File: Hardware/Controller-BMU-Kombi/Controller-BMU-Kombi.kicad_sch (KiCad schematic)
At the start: 45 parts, among them J1 Conn_01x05_Socket, J10 Conn_01x03_Pin, J11 Conn_01x03_Pin, J12 Conn_01x03_Pin, J13 Conn_01x03_Pin, J14 Conn_01x03_Pin, J15 Conn_01x03_Pin, J16 Conn_01x03_Pin, J17 Conn_01x03_Pin, J18 Conn_01x03_Pin, J19 Conn_01x03_Pin, J2 Conn_01x05_Socket, J20 Conn_01x03_Pin, J21 Conn_01x03_Pin, J22 Conn_01x03_Pin, J23 Conn_01x03_Pin, J24 Conn_01x03_Pin, J25 Conn_01x03_Socket, J26 Conn_01x04_Socket, J3 Conn_01x05_Socket, J4 Conn_01x05_Socket, J5 Conn_01x05_Socket, J6 Conn_01x05_Socket, J7 Conn_01x03_Pin, J8 Conn_01x03_Pin, J9 Conn_01x03_Pin, U2 ESP32_NODEMCU, U9 PCA9555PW

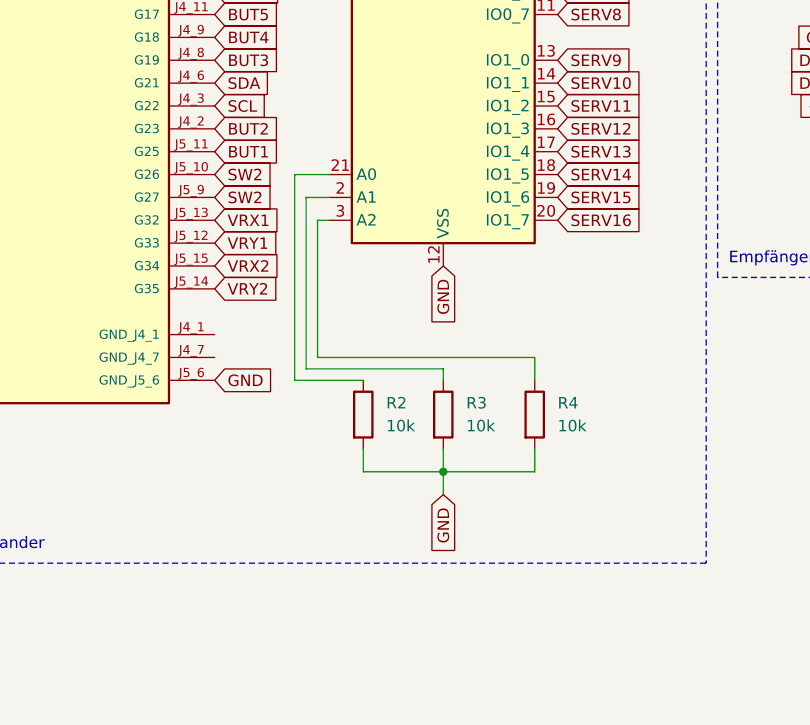
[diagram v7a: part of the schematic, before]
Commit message: Finished Controller-BMU-Kombi PCB
routing finished + finishing touches applied
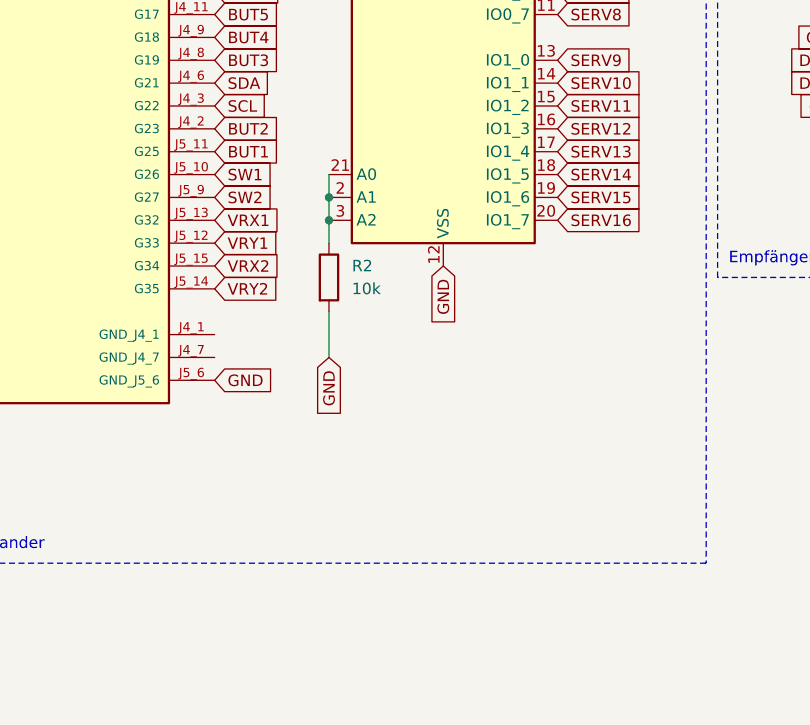
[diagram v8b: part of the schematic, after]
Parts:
- removed R3, R4: 10k, Resistor_SMD:R_1206_3216Metric, symbol Device:R
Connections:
- net SW1: now also U2.J5_10 (G26)
- net SW2: no longer U2.J5_10 (G26)
- net at U9.3 (A2): now also R2.1, U9.2 (A1), U9.21 (A0)
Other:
- moved on the sheet: R2
